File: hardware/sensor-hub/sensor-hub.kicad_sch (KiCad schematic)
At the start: 2 parts, among them J5 Conn_01x10, J6 Conn_01x04

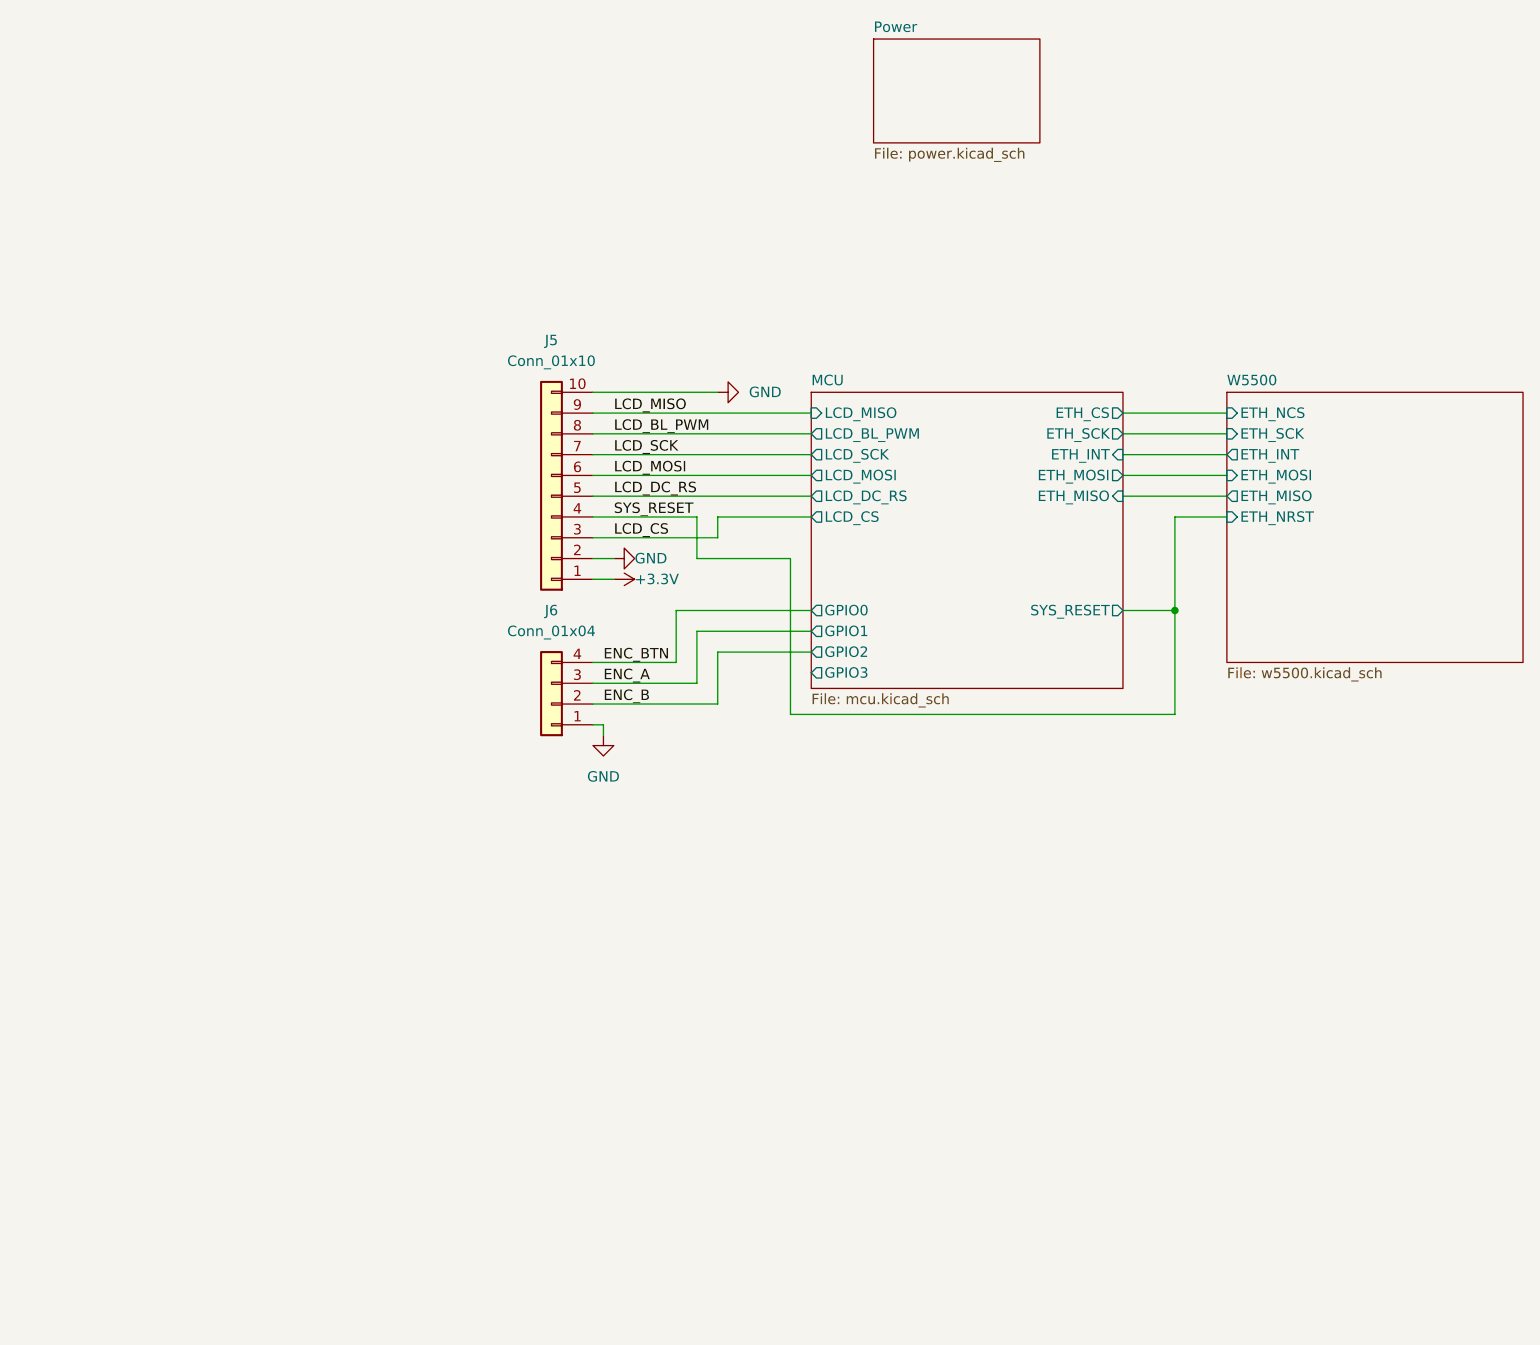
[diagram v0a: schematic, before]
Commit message: Add sensors, connectors
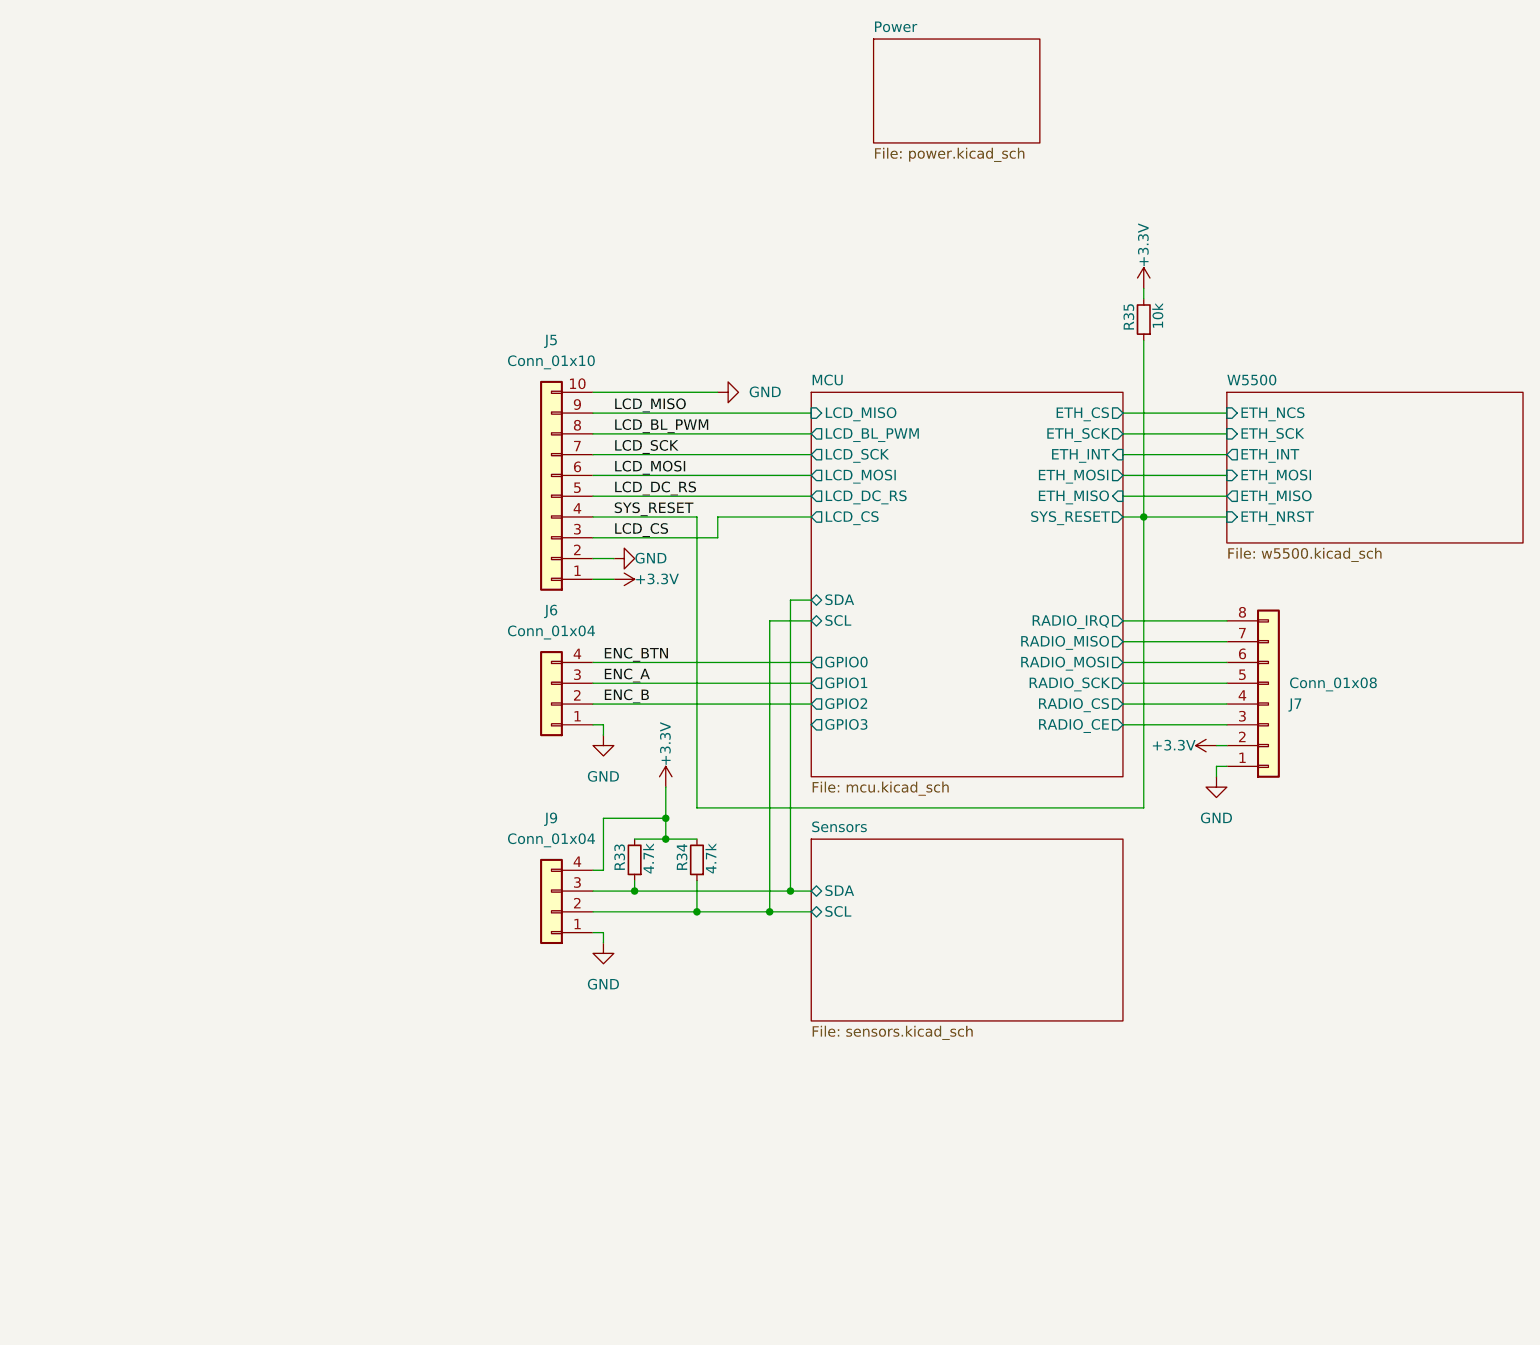
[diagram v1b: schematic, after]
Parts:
- added J7: Conn_01x08, symbol Connector_Generic:Conn_01x08
- added J9: Conn_01x04, symbol Connector_Generic:Conn_01x04
- added R33, R34: 4.7k, symbol Device:R_Small
- added R35: 10k, symbol Device:R_Small
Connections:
- net +3.3V: now also J7.2 (Pin_2), J9.4 (Pin_4), R33.2, R34.2, R35.2
- net GND: now also J7.1 (Pin_1), J9.1 (Pin_1)
- net SYS_RESET: now also R35.1
- new net MCU/RADIO_CE: J7.3 (Pin_3)
- new net MCU/RADIO_CS: J7.4 (Pin_4)
- new net MCU/RADIO_IRQ: J7.8 (Pin_8)
- new net MCU/RADIO_MISO: J7.7 (Pin_7)
- new net MCU/RADIO_MOSI: J7.6 (Pin_6)
- new net MCU/RADIO_SCK: J7.5 (Pin_5)
- new net MCU/SCL: J9.2 (Pin_2), R34.1
- new net MCU/SDA: J9.3 (Pin_3), R33.1
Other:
- added sheet Sensors (sensors.kicad_sch)
- sheet MCU ports: added RADIO_CE, RADIO_CS, RADIO_IRQ, RADIO_MISO, RADIO_MOSI, RADIO_SCK, SCL, SDA; removed none

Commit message: Change crystal packages, assign footprints
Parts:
- J5: footprint (none) -> Connector_TE-Connectivity:TE_Micro-MaTch_1-215079-0_2x05_P1.27mm_Vertical
- J6: footprint (none) -> Connector_TE-Connectivity:TE_Micro-MaTch_215079-4_2x02_P1.27mm_Vertical
- J7: footprint (none) -> Connector_TE-Connectivity:TE_Micro-MaTch_1-215079-6_2x04_P1.27mm_Vertical
- J9: footprint (none) -> Connector_PinHeader_2.54mm:PinHeader_1x04_P2.54mm_Vertical
- R33, R34, R35: footprint (none) -> Resistor_SMD:R_0603_1608Metric
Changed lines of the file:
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@@
 			)
 		)
-		(property "Footprint" ""
+		(property "Footprint" "Connector_TE-Connectivity:TE_Micro-MaTch_1-215079-0_2x05_P1.27mm_Vertical"
 			(at 95.25 76.2 0)
 			(effects
@@
 			)
 		)
-		(property "Footprint" ""
+		(property "Footprint" "Resistor_SMD:R_0603_1608Metric"
 			(at 167.64 54.61 0)
 			(effects
@@
 			)
 		)
-		(property "Footprint" ""
+		(property "Footprint" "Resistor_SMD:R_0603_1608Metric"
 			(at 113.03 120.65 0)
 			(effects
@@
 			)
 		)
-		(property "Footprint" ""
+		(property "Footprint" "Connector_PinHeader_2.54mm:PinHeader_1x04_P2.54mm_Vertical"
 			(at 95.25 127 0)
 			(effects
@@
 			)
 		)
-		(property "Footprint" ""
+		(property "Footprint" "Connector_TE-Connectivity:TE_Micro-MaTch_215079-4_2x02_P1.27mm_Vertical"
 			(at 95.25 101.6 0)
 			(effects
@@
 			)
 		)
-		(property "Footprint" ""
+		(property "Footprint" "Resistor_SMD:R_0603_1608Metric"
 			(at 105.41 120.65 0)
 			(effects
@@
 			)
 		)
-		(property "Footprint" ""
+		(property "Footprint" "Connector_TE-Connectivity:TE_Micro-MaTch_1-215079-6_2x04_P1.27mm_Vertical"
 			(at 182.88 101.6 0)
 			(effects

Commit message: Assign remaining footprints, change HT sensor
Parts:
- J7: footprint Connector_TE-Connectivity:TE_Micro-MaTch_1-215079-6_2x04_P1.27mm_Vertical -> Connector_TE-Connectivity:TE_Micro-MaTch_215079-8_2x04_P1.27mm_Vertical
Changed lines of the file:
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@@
 			)
 		)
-		(property "Footprint" "Connector_TE-Connectivity:TE_Micro-MaTch_1-215079-6_2x04_P1.27mm_Vertical"
+		(property "Footprint" "Connector_TE-Connectivity:TE_Micro-MaTch_215079-8_2x04_P1.27mm_Vertical"
 			(at 182.88 101.6 0)
 			(effects

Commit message: Start layout
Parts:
- added H1, H2, H3, H4: MountingHole, MountingHole:MountingHole_3mm, symbol Mechanical:MountingHole
- J5: value Conn_01x10 -> LCD_CONN
- J6: value Conn_01x04 -> ENC_CONN
- J7: value Conn_01x08 -> RADIO_CONN
- J9: value Conn_01x04 -> I2C_CONN
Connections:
- no-connect marks 0 -> 1

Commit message: Most layout done
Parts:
- added TP1: TestPoint, TestPoint:TestPoint_Pad_D1.0mm, symbol Connector:TestPoint
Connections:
- net MCU/GPIO3: now also TP1.1
- no-connect marks 1 -> 0
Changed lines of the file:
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@@
 		(color 0 0 0 0)
 	)
-	(no_connect
-		(at 127 104.14)
-	)
 	(wire
 		(pts
@@
 		(pts
 			(xy 165.1 93.98) (xy 177.8 93.98)
+		)
+		(stroke
+			(width 0)
+			(type default)
+		)
+	)
+	(wire
+		(pts
+			(xy 119.38 104.14) (xy 127 104.14)
 		)
 		(stroke
@@
 					(unit 1)
 				)
+			)
+		)
+	)
+	(symbol
+		(lib_id "Connector:TestPoint")
+		(at 119.38 104.14 180)
+		(unit 1)
+		(exclude_from_sim no)
+		(in_bom yes)
+		(on_board yes)
+		(dnp no)
+		(property "Reference" "TP1"
+			(at 117.348 107.696 90)
+			(effects
+				(font
+					(size 1.27 1.27)
+				)
+			)
+		)
+		(property "Value" "TestPoint"
+			(at 116.84 107.442 90)
+			(effects
+				(font
+					(size 1.27 1.27)
+				)
+				(hide yes)
+			)
+		)
+		(property "Footprint" "TestPoint:TestPoint_Pad_D1.0mm"
+			(at 114.3 104.14 0)
+			(effects
+				(font
+					(size 1.27 1.27)
+				)
+				(hide yes)
+			)
+		)
+		(property "Datasheet" "~"
+			(at 114.3 104.14 0)
+			(effects
+				(font
+					(size 1.27 1.27)
+				)
+				(hide yes)
+			)
+		)
+		(property "Description" "test point"
+			(at 119.38 104.14 0)
+			(effects
+				(font
+					(size 1.27 1.27)
+				)
+				(hide yes)
+			)
+		)
+		(pin "1"
+		)
+		(instances
+			(project "sensor-hub"
+				(path "/e168ef7b-16e4-493f-b63c-2f69374fc890"
+					(reference "TP1")
+					(unit 1)
+				)
